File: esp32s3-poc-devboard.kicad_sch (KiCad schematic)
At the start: 45 parts, among them J1 24VDC, J2 Conn_01x01_Pin, Q3 MMDT5551, U1 ESP32-S3, U2 AMS1117-3.3, U3 XC6206P332MR, U4 TPS5430DDA

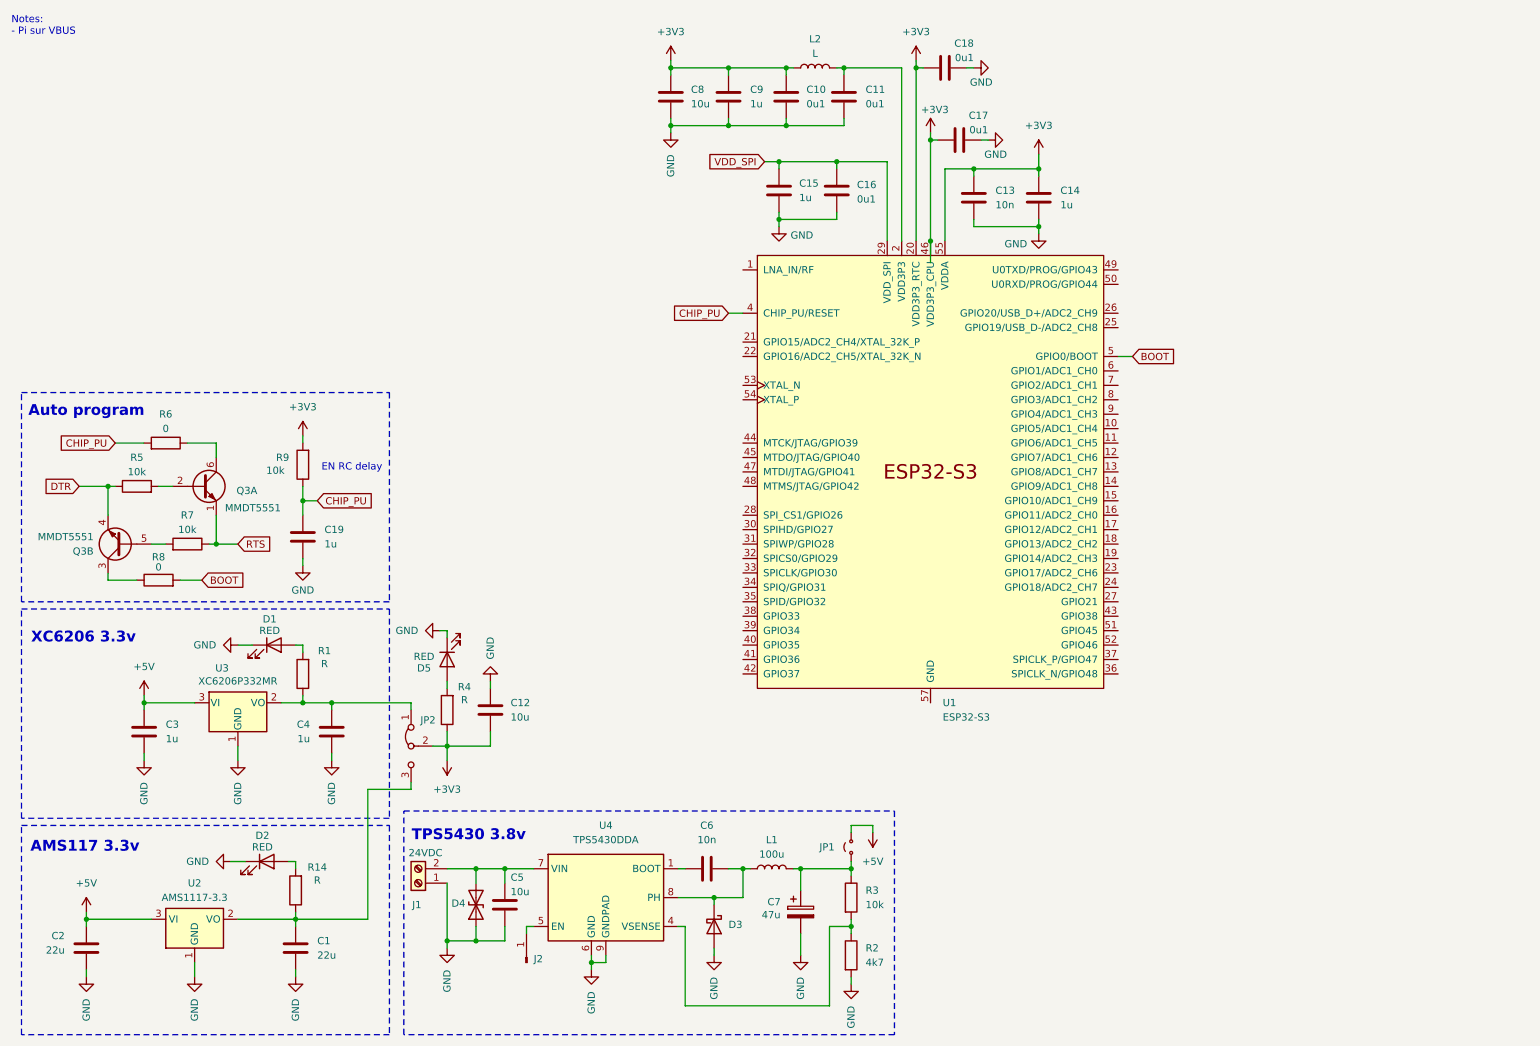
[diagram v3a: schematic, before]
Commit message: add CP2102N usb to uart
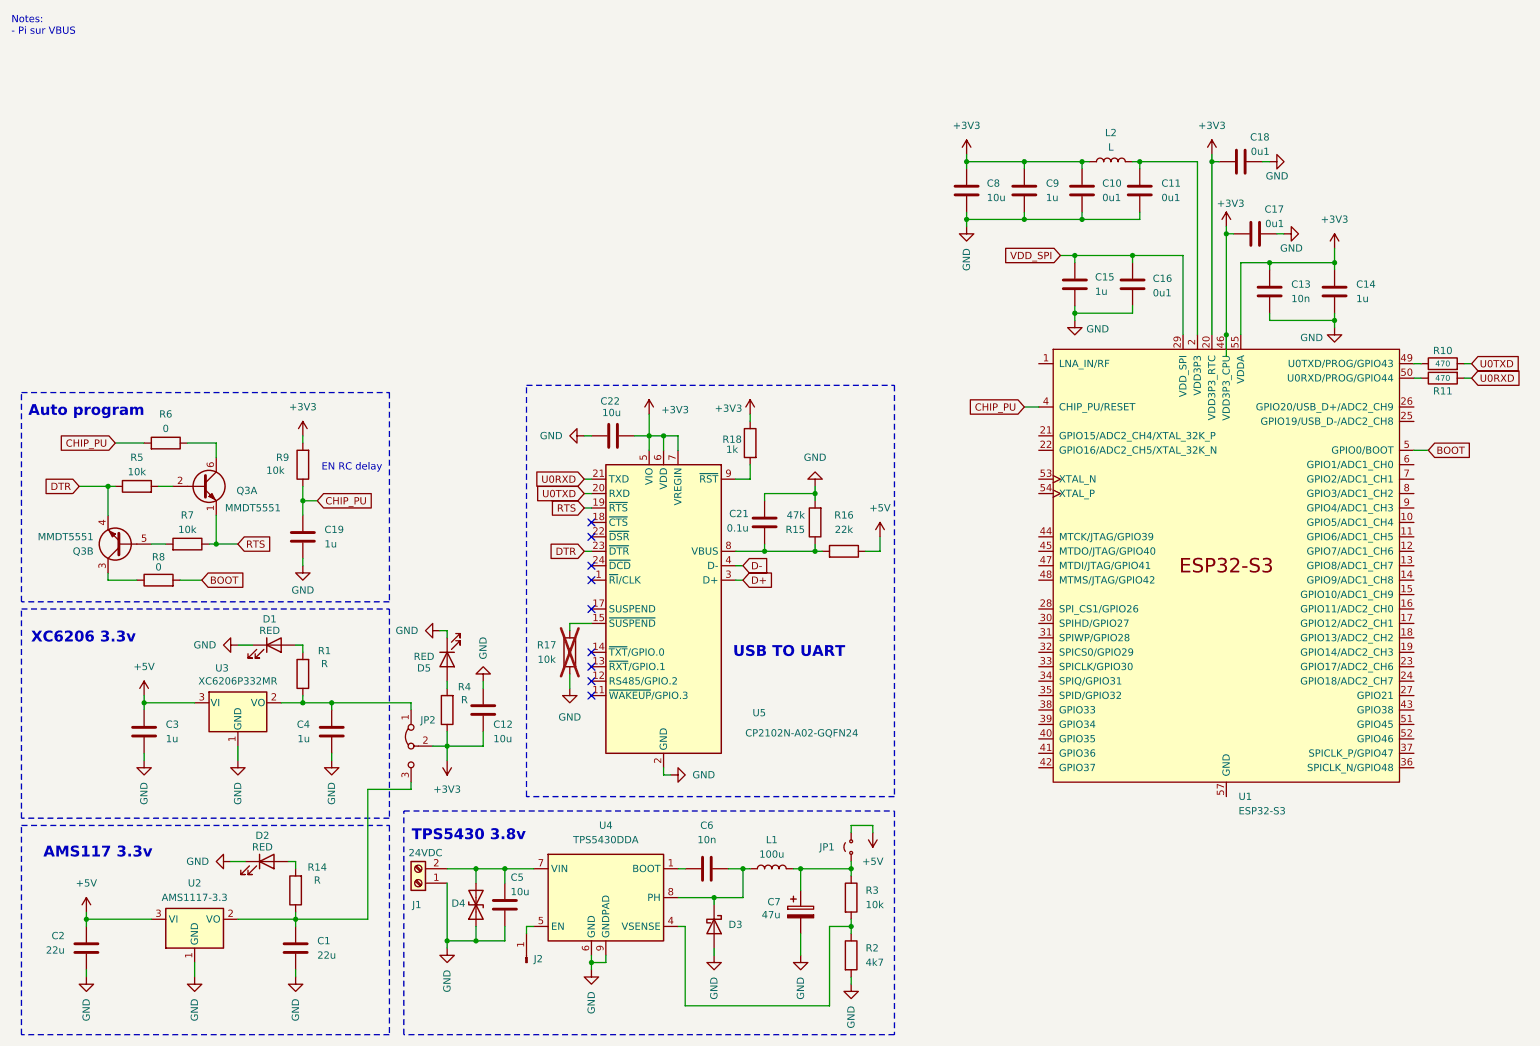
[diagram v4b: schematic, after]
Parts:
- added C21: 0.1u, symbol Device:C
- added C22: 10u, symbol Device:C
- added R10, R11: 470, symbol Device:R
- added R15: 47k, symbol Device:R
- added R16: 22k, symbol Device:R
- added R17: 10k, symbol Device:R
- added R18: 1k, symbol Device:R
- added U5: CP2102N-A02-GQFN24, Package_DFN_QFN:QFN-24-1EP_4x4mm_P0.5mm_EP2.6x2.6mm, symbol Interface_USB:CP2102N-Axx-xQFN24
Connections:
- net +3V3: now also C22.2, R18.1, U5.5 (VIO), U5.6 (VDD), U5.7 (VREGIN)
- net +5V: now also R16.1
- net DTR: now also U5.23 (~{DTR})
- net GND: now also C21.1, C22.1, R15.2, R17.2, U5.2 (GND), U5.25 (GND)
- net RTS: now also U5.19 (~{RTS})
- net at U1.49 (U0TXD/PROG/GPIO43): now also R10.1
- net at U1.50 (U0RXD/PROG/GPIO44): now also R11.1
- new net: C21.2, R15.1, R16.2, U5.8 (VBUS)
- new net: R18.2, U5.9 (~{RST})
- new net: R17.1, U5.15 (~{SUSPEND})
- new net D+: U5.3 (D+)
- new net D-: U5.4 (D-)
- new net U0RXD: R11.2, U5.21 (TXD)
- new net U0TXD: R10.2, U5.20 (RXD)
- no-connect marks 0 -> 9
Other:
- note added: "USB TO UART"
- moved on the sheet: C10, C11, C12, C13, C14, C15, C16, C17, C18, C8, C9, L2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

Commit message: add missing esp32 gnd
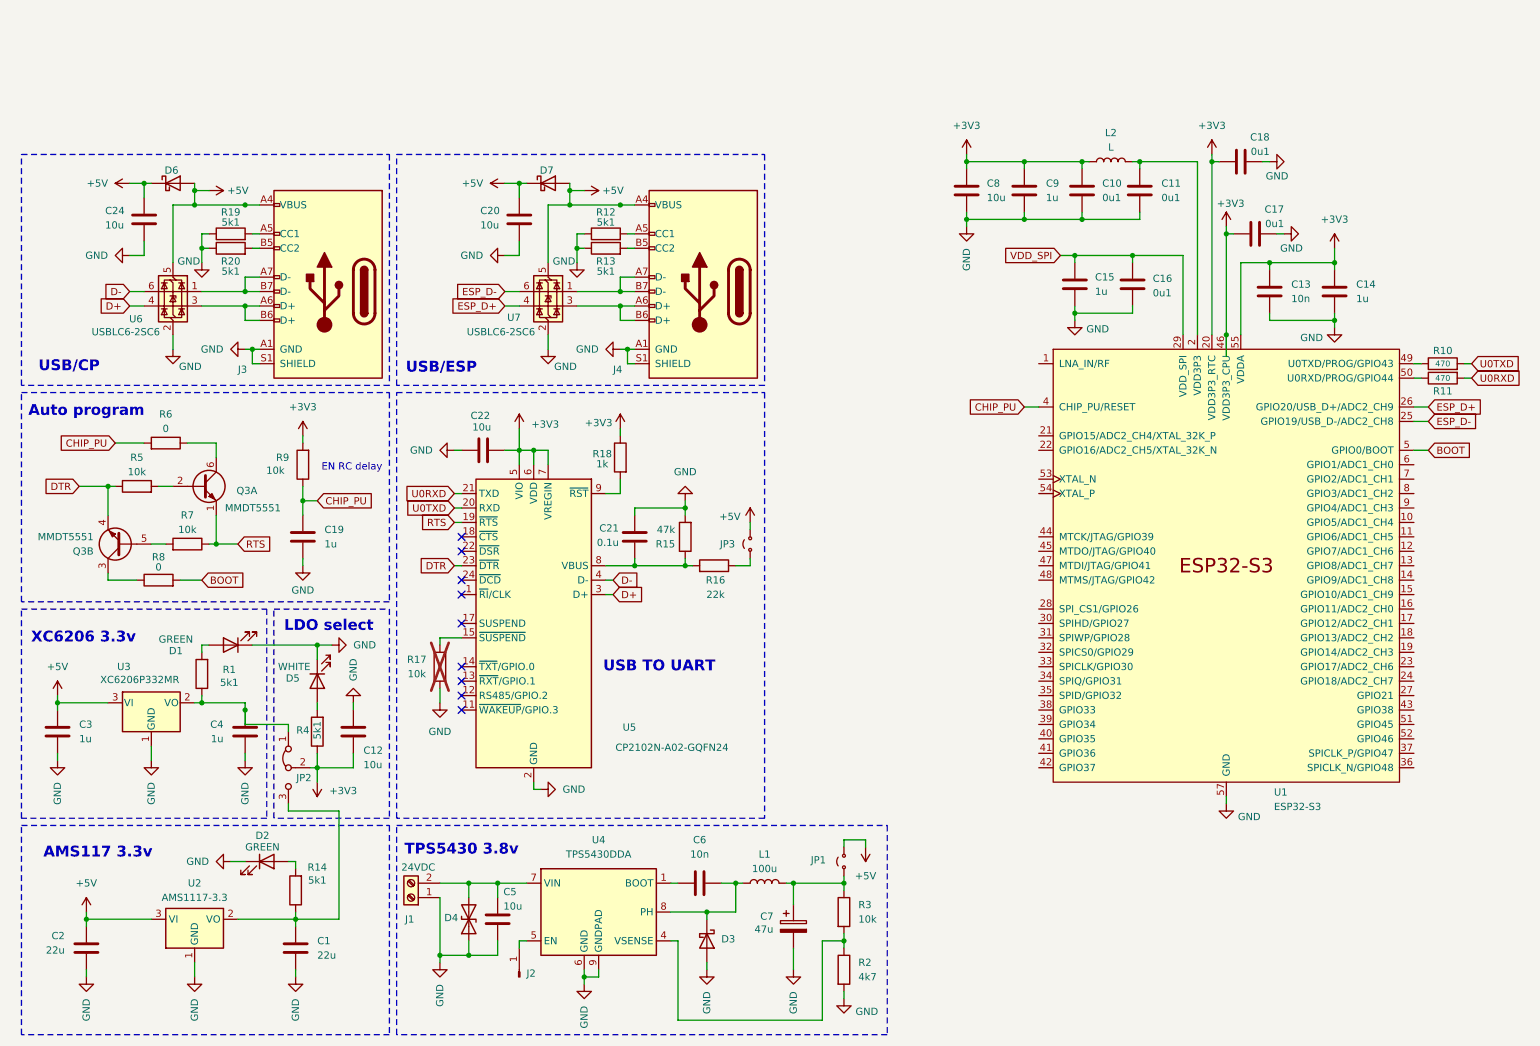
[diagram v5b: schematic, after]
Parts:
- added C20, C24: 10u, symbol Device:C
- added D6, D7: D_Schottky, symbol Device:D_Schottky
- added J3, J4: USB_C_Receptacle_USB2.0_14P, symbol Connector:USB_C_Receptacle_USB2.0_14P
- added JP3: Jumper_2_Small_Open, symbol Jumper:Jumper_2_Small_Open
- added R12, R13, R19, R20: 5k1, symbol Device:R
- added U6, U7: USBLC6-2SC6, Package_TO_SOT_SMD:SOT-23-6, symbol Power_Protection:USBLC6-2SC6
- D1, D2: value RED -> GREEN
- D5: value RED -> WHITE
- R1, R14, R4: value R -> 5k1
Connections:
- net +5V: now also C20.1, C24.1, D6.1 (K), D6.2 (A), D7.1 (K), D7.2 (A), J3.A4 (VBUS), J3.A9 (VBUS), J3.B4 (VBUS), J3.B9 (VBUS), J4.A4 (VBUS), J4.A9 (VBUS), J4.B4 (VBUS), J4.B9 (VBUS), JP3.2 (B), U6.5 (VBUS), U7.5 (VBUS); no longer R16.1
- net D+: now also U6.4 (I/O2)
- net D-: now also U6.6 (I/O1)
- net GND: now also U1.57 (GND), C20.2, C24.2, J3.A1 (GND), J3.S1 (SHIELD), J4.A1 (GND), J4.S1 (SHIELD), R12.1, R13.1, R19.1, R20.1, U6.2 (GND), U7.2 (GND)
- net ESP_D-: now reaches U1.25 (GPIO19/USB_D-/ADC2_CH8)
- net ESP_D-: now also U7.6 (I/O1)
- net ESP_D+: now reaches U1.26 (GPIO20/USB_D+/ADC2_CH9)
- net ESP_D+: now also U7.4 (I/O2)
- new net: J4.A5 (CC1), R12.2
- new net: J4.A6 (D+), J4.B6 (D+), U7.3 (I/O2)
- new net: J4.A7 (D-), J4.B7 (D-), U7.1 (I/O1)
- new net: J4.B1 (GND), J4.B12 (GND)
- new net: J4.B5 (CC2), R13.2
- new net: J3.A5 (CC1), R19.2
- new net: J3.A6 (D+), J3.B6 (D+), U6.3 (I/O2)
- new net: J3.A7 (D-), J3.B7 (D-), U6.1 (I/O1)
- new net: J3.B1 (GND), J3.B12 (GND)
- new net: J3.B5 (CC2), R20.2
- new net: JP3.1 (A), R16.1
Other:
- note added: "LDO select"
- note added: "USB/CP"
- note added: "USB/ESP"
- note removed: "Notes: - Pi sur VBUS"
- moved on the sheet: C12, C21, C22, C3, C4, C5, C6, C7, D1, D3, D4, D5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

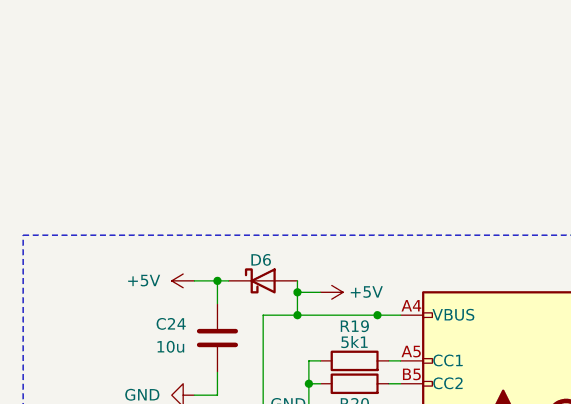
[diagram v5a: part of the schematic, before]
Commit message: add rst/boot buttons
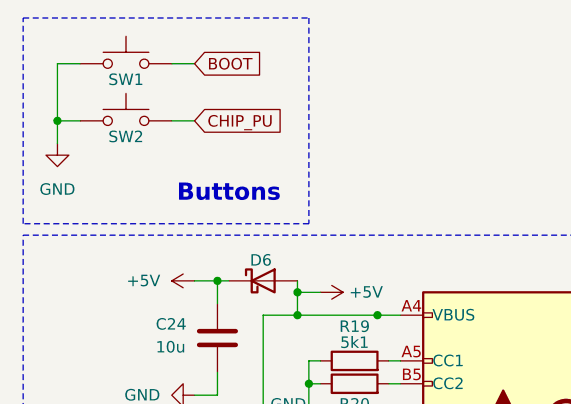
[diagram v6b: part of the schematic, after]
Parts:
- added SW1, SW2: SW_Push, symbol Switch:SW_Push
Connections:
- net BOOT: now also SW1.2
- net CHIP_PU: now also SW2.2
- net GND: now also SW1.1, SW2.1
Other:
- note added: "Buttons"
